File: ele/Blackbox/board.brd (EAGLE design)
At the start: 160 x 119 mm, 77 parts, among them IC1 DS3231/SO, U1 MPU-6050

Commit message: blackbox-sch
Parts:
- removed JP1: (no value), pinhead:1X08
- added R1, R4, R5: (no value), rcl:R0603
- added U$62: EC11-1S, EC11-1S:EC11-1S
- moved JP2 21.6 mm to (77.5, 85.1), flipped to the bottom
- moved C3 16.9 mm to (40.0, 86.4)
- moved C2 16.9 mm to (35.0, 92.7)
- moved C4 16.9 mm to (35.6, 82.5)
- moved C5 16.9 mm to (33.0, 82.5)
- moved U1 16.9 mm to (34.3, 87.6)
- moved IM6 1.27 mm to (29.2, 31.8)
- flipped JP3 to the bottom
- flipped JP4 to the bottom
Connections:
- new net ENC-A: IM6.30, R4.1, U$62.A
- new net ENC-B: IM6.28, R5.1, U$62.B
- new net SW0: IM6.29, R1.1, U$62.P$4
- net +3V3: now also R1.2, R4.2, R5.2; no longer JP1.1
- net ADO: no longer JP1.7
- net GND: now also U$62.IN, U$62.P$5; no longer JP1.2
- net INT: no longer JP1.8
- net RX-GPS: now also IM6.27
- net SCL: no longer JP1.3
- net SDA: no longer JP1.4
- net TX-GPS: now also IM6.26
- net XCL: no longer JP1.6
- net XDA: no longer JP1.5

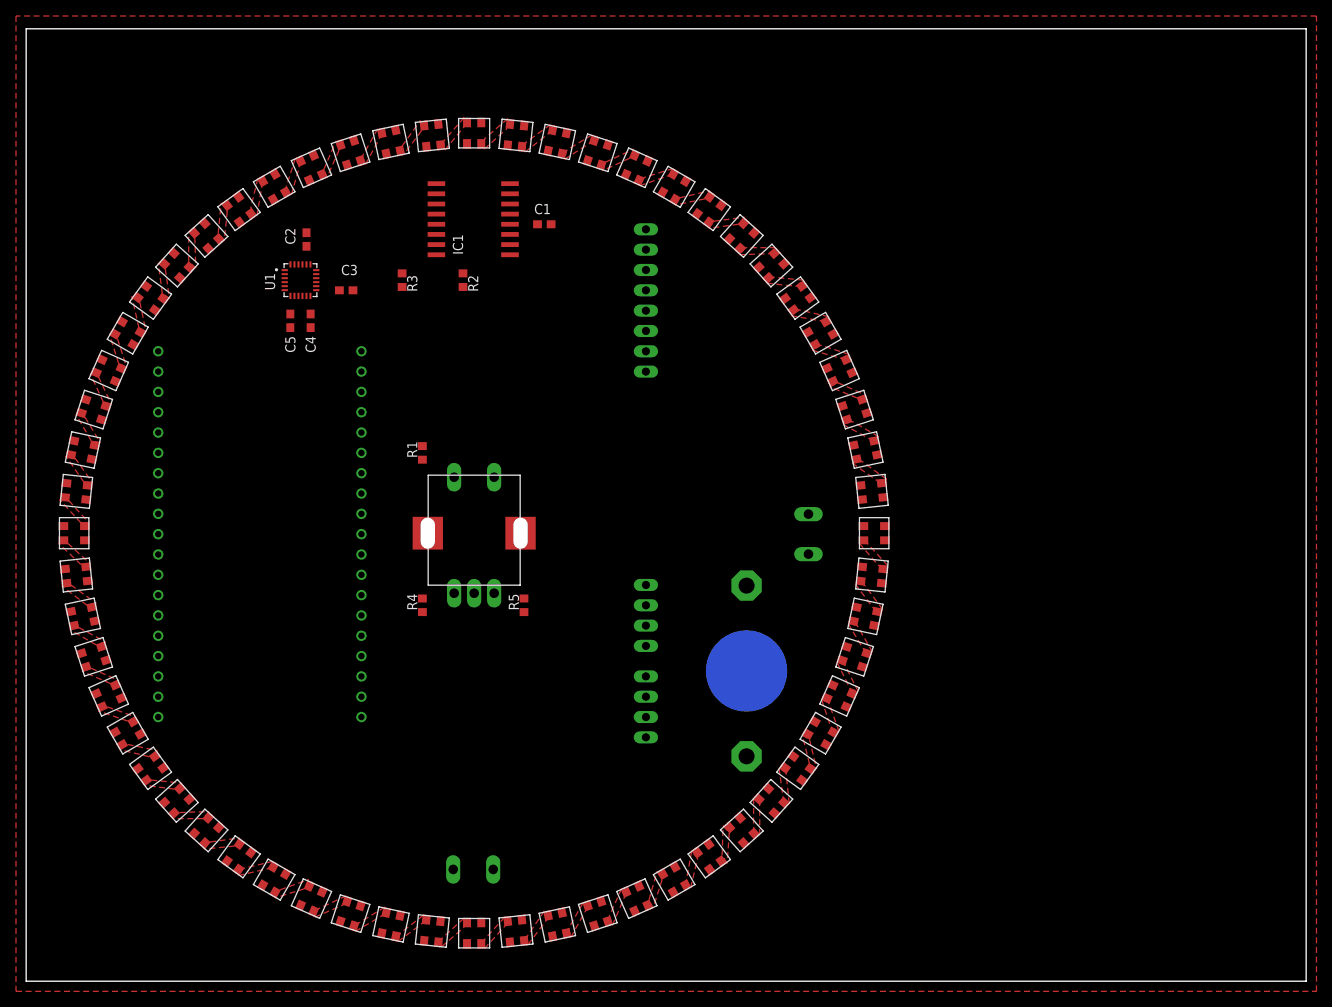
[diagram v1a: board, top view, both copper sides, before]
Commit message: max485
-max485
-nejake datashity pouzitych soucastek
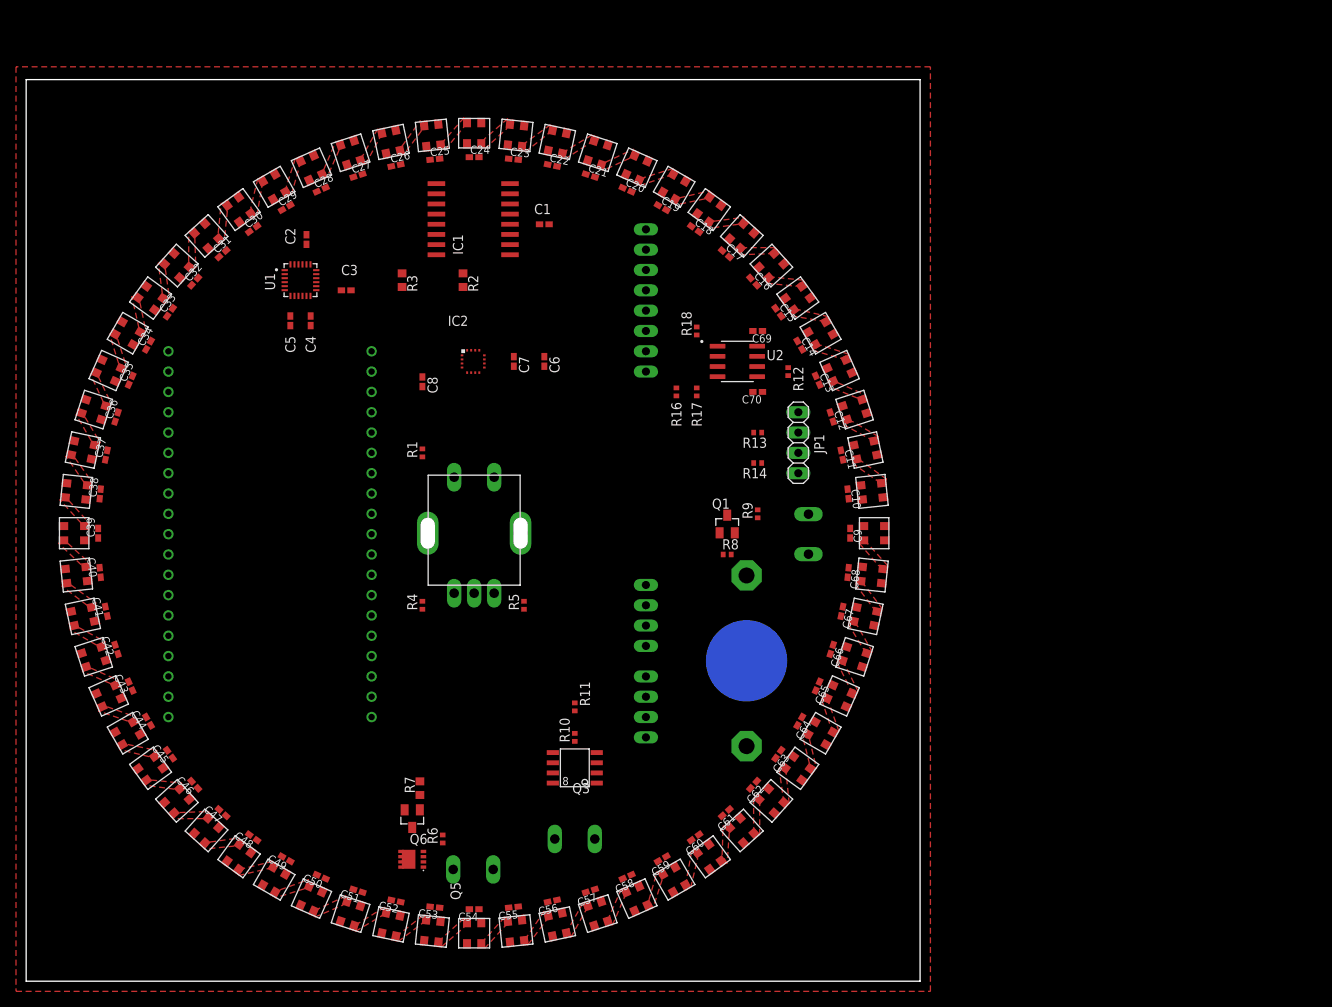
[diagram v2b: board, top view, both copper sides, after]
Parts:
- added C10, C11, C12, C13, C14, C15, C16, C17, C18, C19, C20, C21, C22, C23, C24, C25, C26, C27, C28, C29, C30, C31, C32, C33, C34, C35, C36, C37, C38, C39, C40, C41, C42, C43, C44, C45, C46, C47, C48, C49, C50, C51, C52, C53, C54, C55, C56, C57, C58, C59, C60, C61, C62, C63, C64, C65, C66, C67, C68, C9: (no value), rcl:C0402K
- added C6: 0.22uf, rcl:C0402K
- added C69, C70: 10uf, rcl:C0402K
- added C7: 4.7uf, rcl:C0402K
- added C8: 0.1uf, rcl:C0402K
- added IC2: QMC5883L-TR, QMC5883L-TR:QMC5882L-TR
- added JP1: (no value), pinhead:1X04
- added MOTOR: (no value), con-wago-500:W237-102
- added Q1, Q6: (no value), transistors:SOT23
- added Q3: (no value), transistors:SO-8
- added Q5: (no value), transistors:MLP3.3X3.3
- added R10, R12: 220, rcl:R0402
- added R11: 100k, rcl:R0402
- added R13, R14: 20k, rcl:R0402
- added R16, R17, R18, R8, R9: 10k, rcl:R0402
- added R6: 1M, rcl:R0402
- added R7: 220, rcl:R0603
- added U2: MAX485ESA+, MAX485ESA_:SOIC127P600X175-8N
- C1, C2, C3, C4, C5: device rcl:C0603 -> rcl:C0402K
- R1, R4, R5: value (none) -> 10k; device rcl:R0603 -> rcl:R0402
- moved IM6 1.27 mm to (30.5, 31.8)
- moved U$1 1.27 mm to (90.0, 40.0)
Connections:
- removed net !GND: U$10.GND, U$11.GND, U$12.GND, U$13.GND, U$14.GND, U$15.GND, U$16.GND, U$17.GND, U$18.GND, U$19.GND, U$2.GND, U$20.GND, U$21.GND, U$22.GND, U$23.GND, U$24.GND, U$25.GND, U$26.GND, U$27.GND, U$28.GND, U$29.GND, U$3.GND, U$30.GND, U$31.GND, U$32.GND, U$33.GND, U$34.GND, U$35.GND, U$36.GND, U$37.GND, U$38.GND, U$39.GND, U$4.GND, U$40.GND, U$41.GND, U$42.GND, U$43.GND, U$44.GND, U$45.GND, U$46.GND, U$47.GND, U$48.GND, U$49.GND, U$5.GND, U$50.GND, U$51.GND, U$52.GND, U$53.GND, U$54.GND, U$55.GND, U$56.GND, U$57.GND, U$58.GND, U$59.GND, U$6.GND, U$60.GND, U$61.GND, U$7.GND, U$8.GND, U$9.GND
- new net IO10_NC2: IC2.5
- new net IO10_NC3: IC2.3
- new net IO9_NC2: IC2.14
- new net IO9_NC3: IC2.7
- new net LED-SHUTDOWN: IM6.24, R7.2
- new net MODE-485: IM6.25, R16.1, U2.2, U2.3
- new net MOTOR: IM6.13, R10.2
- new net N$60: C6.1, IC2.12
- new net N$62: C6.2, IC2.8
- new net N$66: C7.1, IC2.10
- new net N$68: Q5.4, Q6.3, R6.2
- new net N$69: Q6.1, R7.1
- new net N$70: MOTOR.2, Q3.5, Q3.6, Q3.7, Q3.8
- new net N$71: Q3.4, R10.1, R11.2
- new net N$72: JP1.2, R12.1, R14.1, U2.7
- new net N$73: JP1.3, R12.2, R13.1, U2.6
- new net N$74: Q3.1, Q3.2, Q3.3
- new net QMC5883-INTERRUPT: IC2.15, IM6.15
- new net RX-485: R18.1, U2.1
- new net SQW/INT: IC1.3, IM6.23
- new net TX-485: R17.1, U2.4
- new net VCC: C10.1, C11.1, C12.1, C13.1, C14.1, C15.1, C16.1, C17.1, C18.1, C19.1, C20.1, C21.1, C22.1, C23.1, C24.1, C25.1, C26.1, C27.1, C28.1, C29.1, C30.1, C31.1, C32.1, C33.1, C34.1, C35.1, C36.1, C37.1, C38.1, C39.1, C40.1, C41.1, C42.1, C43.1, C44.1, C45.1, C46.1, C47.1, C48.1, C49.1, C50.1, C51.1, C52.1, C53.1, C54.1, C55.1, C56.1, C57.1, C58.1, C59.1, C60.1, C61.1, C62.1, C63.1, C64.1, C65.1, C66.1, C67.1, C68.1, C9.1, Q5.5, Q5.6, Q5.7, Q5.8, U$10.VCC, U$11.VCC, U$12.VCC, U$13.VCC, U$14.VCC, U$15.VCC, U$16.VCC, U$17.VCC, U$18.VCC, U$19.VCC, U$2.VCC, U$20.VCC, U$21.VCC, U$22.VCC, U$23.VCC, U$24.VCC, U$25.VCC, U$26.VCC, U$27.VCC, U$28.VCC, U$29.VCC, U$3.VCC, U$30.VCC, U$31.VCC, U$32.VCC, U$33.VCC, U$34.VCC, U$35.VCC, U$36.VCC, U$37.VCC, U$38.VCC, U$39.VCC, U$4.VCC, U$40.VCC, U$41.VCC, U$42.VCC, U$43.VCC, U$44.VCC, U$45.VCC, U$46.VCC, U$47.VCC, U$48.VCC, U$49.VCC, U$5.VCC, U$50.VCC, U$51.VCC, U$52.VCC, U$53.VCC, U$54.VCC, U$55.VCC, U$56.VCC, U$57.VCC, U$58.VCC, U$59.VCC, U$6.VCC, U$60.VCC, U$61.VCC, U$7.VCC, U$8.VCC, U$9.VCC
- new net WS2812-5V: Q1.3, R9.2, U$61.DIN
- net +3V3: now also C8.1, IC2.13, IC2.2, IC2.S1, Q1.1, R8.1
- net +5V: now also C69.1, C70.1, JP1.4, MOTOR.1, Q5.1, Q5.2, Q5.3, R13.2, R16.2, R17.2, R18.2, R6.1, R9.1, U2.8; no longer U$10.VCC, U$11.VCC, U$12.VCC, U$13.VCC, U$14.VCC, U$15.VCC, U$16.VCC, U$17.VCC, U$18.VCC, U$19.VCC, U$2.VCC, U$20.VCC, U$21.VCC, U$22.VCC, U$23.VCC, U$24.VCC, U$25.VCC, U$26.VCC, U$27.VCC, U$28.VCC, U$29.VCC, U$3.VCC, U$30.VCC, U$31.VCC, U$32.VCC, U$33.VCC, U$34.VCC, U$35.VCC, U$36.VCC, U$37.VCC, U$38.VCC, U$39.VCC, U$4.VCC, U$40.VCC, U$41.VCC, U$42.VCC, U$43.VCC, U$44.VCC, U$45.VCC, U$46.VCC, U$47.VCC, U$48.VCC, U$49.VCC, U$5.VCC, U$50.VCC, U$51.VCC, U$52.VCC, U$53.VCC, U$54.VCC, U$55.VCC, U$56.VCC, U$57.VCC, U$58.VCC, U$59.VCC, U$6.VCC, U$60.VCC, U$61.VCC, U$7.VCC, U$8.VCC, U$9.VCC
- net GND: now also C10.2, C11.2, C12.2, C13.2, C14.2, C15.2, C16.2, C17.2, C18.2, C19.2, C20.2, C21.2, C22.2, C23.2, C24.2, C25.2, C26.2, C27.2, C28.2, C29.2, C30.2, C31.2, C32.2, C33.2, C34.2, C35.2, C36.2, C37.2, C38.2, C39.2, C40.2, C41.2, C42.2, C43.2, C44.2, C45.2, C46.2, C47.2, C48.2, C49.2, C5.2, C50.2, C51.2, C52.2, C53.2, C54.2, C55.2, C56.2, C57.2, C58.2, C59.2, C60.2, C61.2, C62.2, C63.2, C64.2, C65.2, C66.2, C67.2, C68.2, C69.2, C7.2, C70.2, C8.2, C9.2, IC2.11, IC2.9, JP1.1, Q6.2, R11.1, R14.2, U$10.GND, U$11.GND, U$12.GND, U$13.GND, U$14.GND, U$15.GND, U$16.GND, U$17.GND, U$18.GND, U$19.GND, U$2.GND, U$20.GND, U$21.GND, U$22.GND, U$23.GND, U$24.GND, U$25.GND, U$26.GND, U$27.GND, U$28.GND, U$29.GND, U$3.GND, U$30.GND, U$31.GND, U$32.GND, U$33.GND, U$34.GND, U$35.GND, U$36.GND, U$37.GND, U$38.GND, U$39.GND, U$4.GND, U$40.GND, U$41.GND, U$42.GND, U$43.GND, U$44.GND, U$45.GND, U$46.GND, U$47.GND, U$48.GND, U$49.GND, U$5.GND, U$50.GND, U$51.GND, U$52.GND, U$53.GND, U$54.GND, U$55.GND, U$56.GND, U$57.GND, U$58.GND, U$59.GND, U$6.GND, U$60.GND, U$61.GND, U$7.GND, U$8.GND, U$9.GND, U2.5
- net IO11_NC2: now also IC2.6; no longer IC1.3
- net N$3: no longer C5.2
- net SCL: now also IC2.1
- net SDA: now also IC2.16
- net WS2812: now also Q1.2, R8.2; no longer U$61.DIN
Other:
- board size 160 x 119 mm -> 111.7 x 112.7 mm
